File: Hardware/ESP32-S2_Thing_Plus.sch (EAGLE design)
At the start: 66 parts, among them J3 QWIIC_RA, J5 USB-C, J6 JTAG, Q1 2.5A/30V, Q2 MBT3904DW1T1, U1 ESP32-S2-WROOM, U2 CP210X, U3 AP2112, U4 MCP73831, U5 TC7USB40MU, Y1 32.768kHz

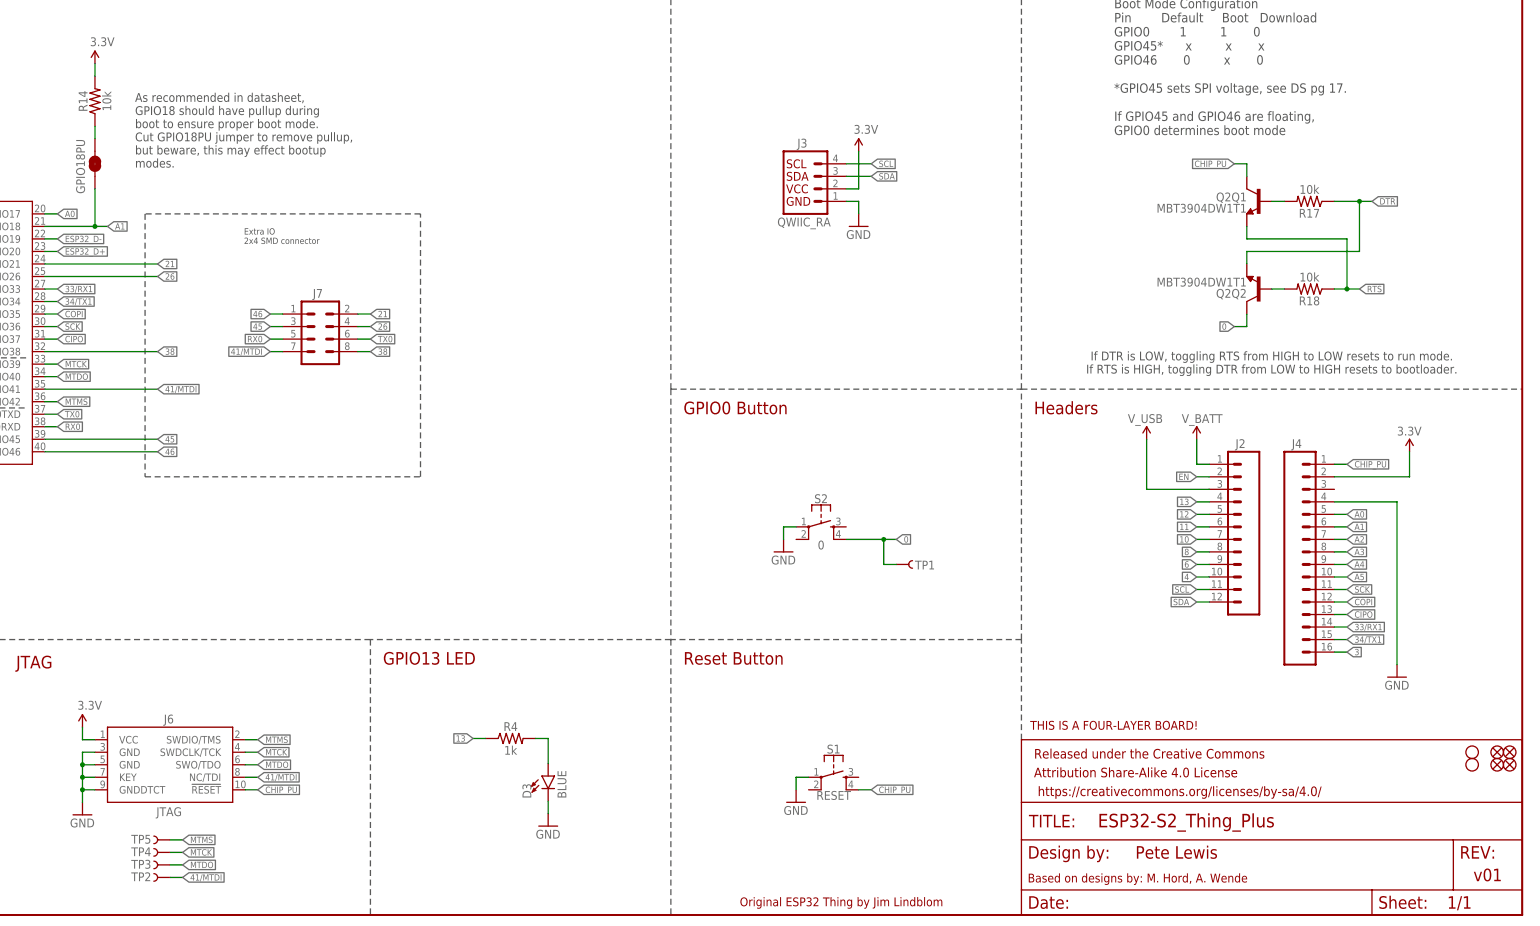
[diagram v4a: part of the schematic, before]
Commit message: v10
-switched to normally open jumper on GPIO18. Testing showed this was unnecessary. (also updated jumper paragraph in schematic).
-bumped version to v10 in both sch and brd.
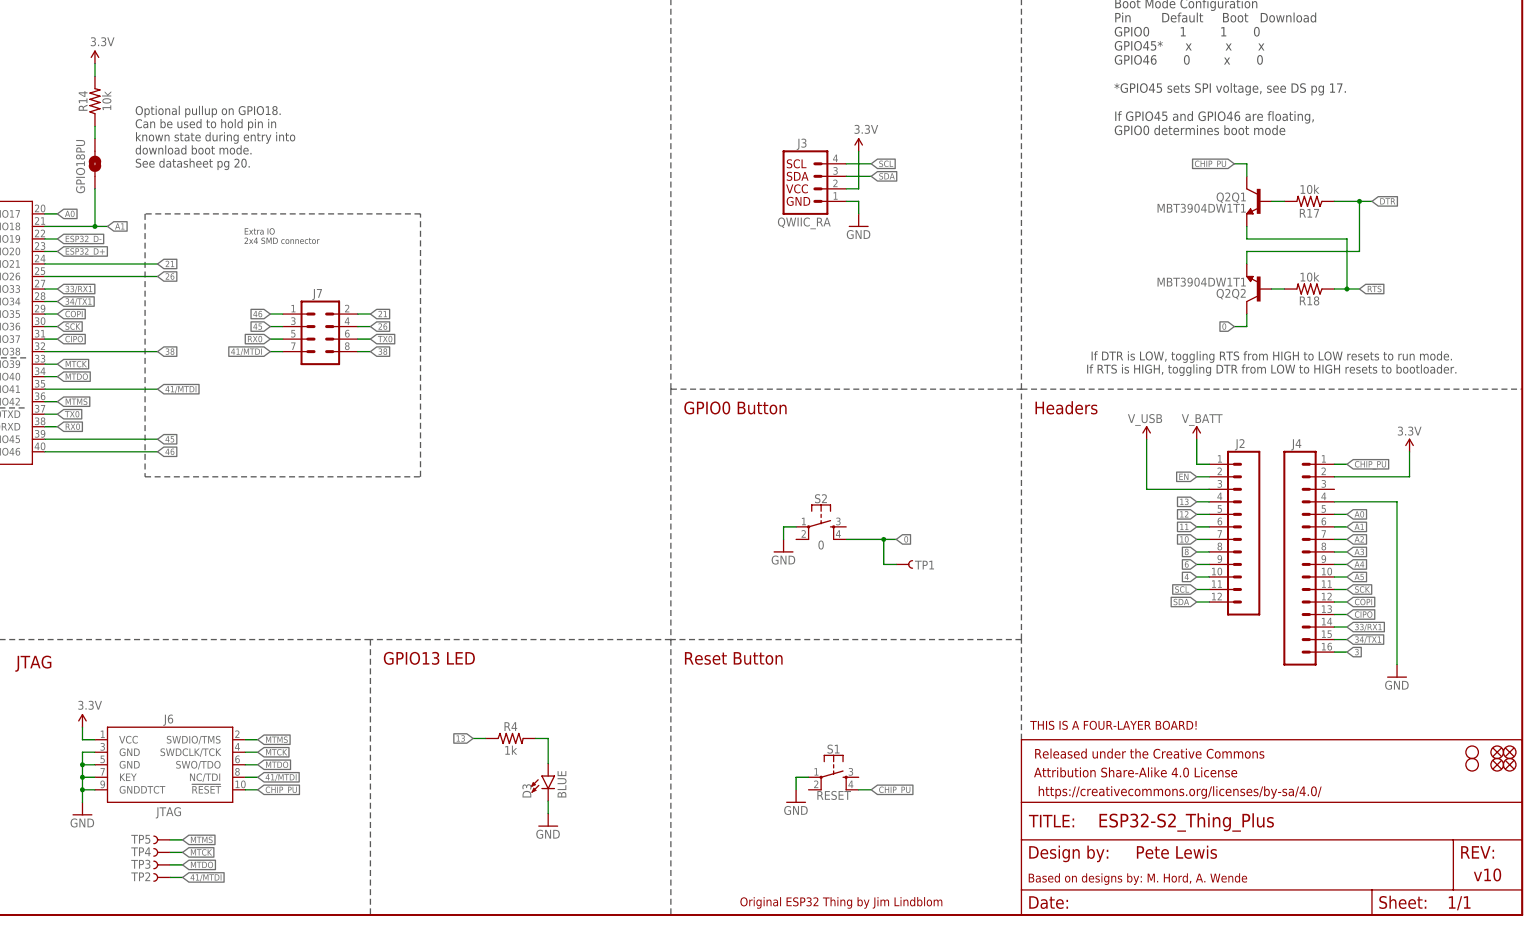
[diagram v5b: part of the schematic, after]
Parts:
- GPIO18PU: value JUMPER-SMT_2_NC_TRACE_SILK -> JUMPER-SMT_2_NO_SILK; device SparkFun-Jumpers:JUMPER-SMT_2_NC_TRACE_SILK -> SparkFun-Jumpers:JUMPER-SMT_2_NO_SILK
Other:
- note added: "Optional pullup on GPIO18. Can be used to hold pin in known state during entry into download boot mode. See datasheet pg 20."
- note added: "v10"
- note removed: "As recommended in datasheet, GPIO18 should have pullup during boot to ensure proper boot mode. Cut GPIO18PU jumper to remove pullup, but beware, this may effect bootup modes."
- note removed: "v01"

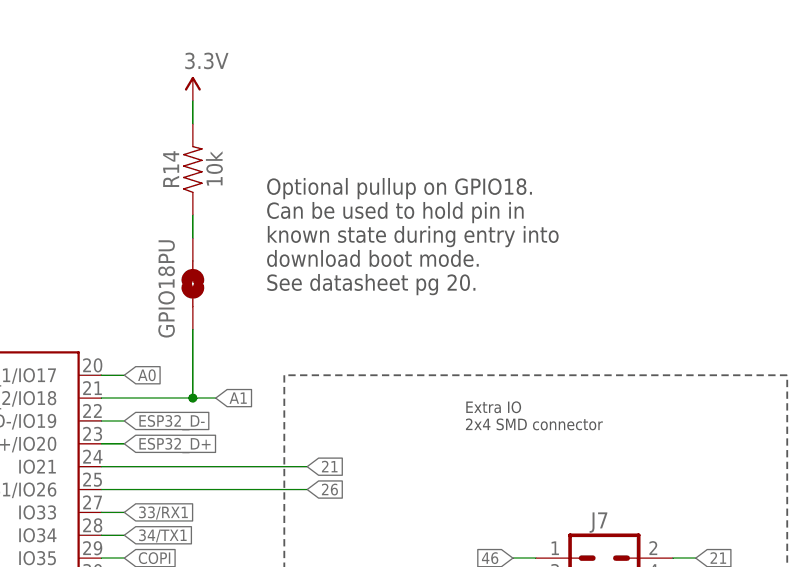
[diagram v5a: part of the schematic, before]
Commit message: datasheet page correction in sch note about GPIO18 jumper
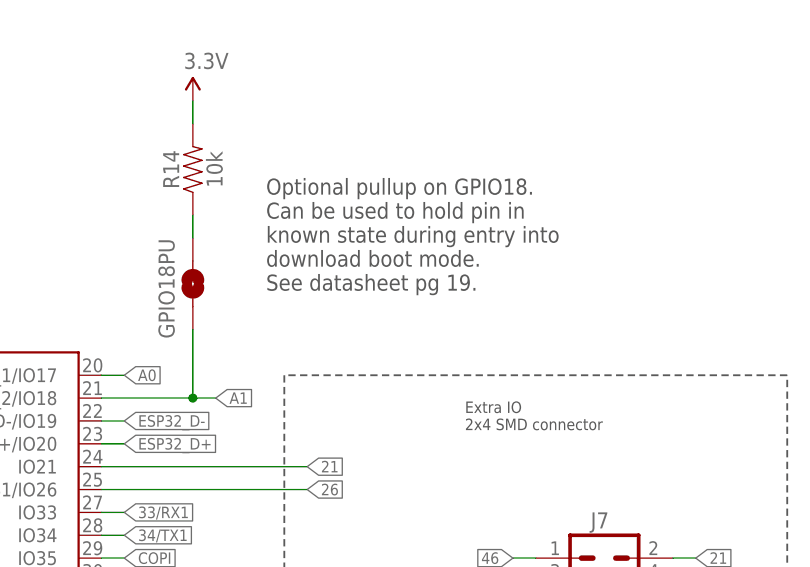
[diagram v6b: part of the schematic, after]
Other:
- note added: "Optional pullup on GPIO18. Can be used to hold pin in known state during entry into download boot mode. See datasheet pg 19."
- note removed: "Optional pullup on GPIO18. Can be used to hold pin in known state during entry into download boot mode. See datasheet pg 20."
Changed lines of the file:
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@@
 known state during entry into
 download boot mode.
-See datasheet pg 20.</text>
+See datasheet pg 19.</text>
 </plain>
 <instances>
